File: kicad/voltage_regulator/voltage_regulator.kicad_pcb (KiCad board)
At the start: 2 copper layers, 135.9 x 78.7 mm, 18 parts

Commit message: New commit.
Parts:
- moved XS2 26.2 mm to (178.4, 96.3)
- moved C6 20.9 mm to (171.4, 122.9)
- moved C3 20.9 mm to (171.4, 89.9)
- moved C2 19.1 mm to (153.0, 80.4)
- moved 1_PIN 18.6 mm to (182.9, 65.8)
- moved FU1 17.8 mm to (101.0, 85.5)
- moved 1_PIN 17.6 mm to (182.9, 122.9)
- moved C1 17.5 mm to (121.9, 80.4)
- moved C5 17.2 mm to (153.0, 112.1)
- moved C4 15.5 mm to (121.9, 112.1)
- moved VD1 13.8 mm to (93.3, 71.5), turned to 180 degrees
- moved FU2 12.8 mm to (101.0, 107.1)
- moved VD2 12.3 mm to (90.2, 80.4), turned to 270 degrees
- moved 1_PIN 11.0 mm to (76.2, 124.8)
- moved XS1 10.0 mm to (91.4, 96.3)
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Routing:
- net /GND: track 180.3 -> 23.5 mm
- net /VCC+: track 146.6 -> 4.45 mm
- net /VCC-: track 142.4 -> 4.32 mm
- net N-000004: track 80.1 -> 59.2 mm
- net N-000006: track 28.8 -> 9.79 mm
- net N-000005: track 28.8 -> 9.90 mm
- net N-000003: track 69.2 -> 59.5 mm
- added copper zone on B.Cu, net /GND
- added copper zone on F.Cu, net /VCC+
- added copper zone on B.Cu, net /VCC-
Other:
- board size 135.9 x 78.7 mm -> 101 x 63.5 mm
- net class Default: clearance 1.00076 -> 0.5; trace_width 0.50038 -> 1
- rule trace_clearance: 1.00076 -> 0.5
- board text added: "GND"
- board text added: "VCC"
- board text added: "VCC+"
- board text added: "VCC-"

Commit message: New commit.
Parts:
- moved VD4 8.00 mm to (93.3, 113.0)
- moved VD1 7.87 mm to (93.3, 79.4)
- moved VD2 2.16 mm to (88.3, 79.4), turned to 180 degrees
- moved VD3 2.10 mm to (88.3, 113.0), turned to 180 degrees
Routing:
- net /GND: track 23.5 -> 47.0 mm
- net N-000004: track 59.2 -> 68.7 mm
- net N-000003: track 59.5 -> 67.9 mm
- added copper zone on F.Cu, net /GND
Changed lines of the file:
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@@
     (thickness 1.6002)
     (drawings 10)
-    (tracks 25)
+    (tracks 29)
     (zones 0)
     (modules 18)
@@
   )
   (module TO220_DIOD_VERT_POZ (layer Front)
-    (at 93.345 121.031 180)
+    (at 93.345 113.03 180)
     (descr "Regulateur TO220 serie LM78xx")
     (tags "TR TO220")
-    (fp_text reference VD4 (at 3.81 3.81 270) (layer F.SilkS)
+    (fp_text reference VD4 (at 0.127 6.223 180) (layer F.SilkS)
       (effects (font (size 1.524 1.016) (thickness 0.2032)))
     )
@@
   )
   (module TO220_DIOD_VERT_POZ (layer Front)
-    (at 93.345 71.501 180)
+    (at 93.345 79.375 180)
     (descr "Regulateur TO220 serie LM78xx")
     (tags "TR TO220")
-    (fp_text reference VD1 (at 3.81 -3.81 270) (layer F.SilkS)
+    (fp_text reference VD1 (at 0 -6.604 180) (layer F.SilkS)
       (effects (font (size 1.524 1.016) (thickness 0.2032)))
     )
@@
   )
   (module TO220_DIOD_VERT_POZ (layer Front)
-    (at 90.17 80.391 270)
+    (at 88.265 79.375 180)
     (descr "Regulateur TO220 serie LM78xx")
     (tags "TR TO220")
-    (fp_text reference VD2 (at 0 6.35 270) (layer F.SilkS)
-      (effects (font (size 1.524 1.016) (thickness 0.2032)))
-    )
-    (fp_text value MDR10100 (at -3.81 0 360) (layer F.SilkS) hide
+    (fp_text reference VD2 (at 0 -6.604 180) (layer F.SilkS)
+      (effects (font (size 1.524 1.016) (thickness 0.2032)))
+    )
+    (fp_text value MDR10100 (at -3.81 0 270) (layer F.SilkS) hide
       (effects (font (size 1.524 1.016) (thickness 0.2032)))
     )
@@
     (fp_line (start 1.905 5.08) (end -1.905 5.08) (layer F.SilkS) (width 0.381))
     (fp_line (start -1.905 5.08) (end -1.905 -5.08) (layer F.SilkS) (width 0.381))
-    (pad 2 thru_hole rect (at 0 -2.54 270) (size 1.778 1.778) (drill 1.00076)
+    (pad 2 thru_hole rect (at 0 -2.54 180) (size 1.778 1.778) (drill 1.00076)
       (layers *.Cu *.Mask F.SilkS)
       (net 2 /VCC+)
     )
-    (pad 1 thru_hole circle (at 0 2.54 270) (size 1.778 1.778) (drill 1.00076)
+    (pad 1 thru_hole circle (at 0 2.54 180) (size 1.778 1.778) (drill 1.00076)
       (layers *.Cu *.Mask F.SilkS)
       (net 5 N-000004)
@@
   )
   (module TO220_DIOD_VERT_POZ (layer Front)
-    (at 90.17 112.141 90)
+    (at 88.265 113.03 180)
     (descr "Regulateur TO220 serie LM78xx")
     (tags "TR TO220")
-    (fp_text reference VD3 (at 0 -6.35 90) (layer F.SilkS)
-      (effects (font (size 1.524 1.016) (thickness 0.2032)))
-    )
-    (fp_text value MDR10100 (at -3.81 0 180) (layer F.SilkS) hide
+    (fp_text reference VD3 (at 0.127 6.35 180) (layer F.SilkS)
+      (effects (font (size 1.524 1.016) (thickness 0.2032)))
+    )
+    (fp_text value MDR10100 (at -3.81 0 270) (layer F.SilkS) hide
       (effects (font (size 1.524 1.016) (thickness 0.2032)))
     )
@@
     (fp_line (start 1.905 5.08) (end -1.905 5.08) (layer F.SilkS) (width 0.381))
     (fp_line (start -1.905 5.08) (end -1.905 -5.08) (layer F.SilkS) (width 0.381))
-    (pad 2 thru_hole rect (at 0 -2.54 90) (size 1.778 1.778) (drill 1.00076)
+    (pad 2 thru_hole rect (at 0 -2.54 180) (size 1.778 1.778) (drill 1.00076)
       (layers *.Cu *.Mask F.SilkS)
       (net 4 N-000003)
     )
-    (pad 1 thru_hole circle (at 0 2.54 90) (size 1.778 1.778) (drill 1.00076)
+    (pad 1 thru_hole circle (at 0 2.54 180) (size 1.778 1.778) (drill 1.00076)
       (layers *.Cu *.Mask F.SilkS)
       (net 3 /VCC-)
@@
   (gr_line (start 182.915 64.516) (end 81.915 64.516) (angle 90) (layer Edge.Cuts) (width 0.381))
   (gr_line (start 81.915 128.016) (end 182.915 128.016) (angle 90) (layer Edge.Cuts) (width 0.381))
-  (gr_text VCC (at 91.44 106.426) (layer F.SilkS)
+  (gr_text VCC (at 85.09 101.6) (layer F.SilkS)
     (effects (font (size 2.032 1.524) (thickness 0.3048)))
   )
   (gr_line (start 182.915 128.016) (end 182.915 64.516) (angle 90) (layer Edge.Cuts) (width 0.381))
   (gr_line (start 81.915 128.016) (end 81.915 64.516) (angle 90) (layer Edge.Cuts) (width 0.381))
-  (gr_text GND (at 85.725 96.266 90) (layer F.SilkS)
+  (gr_text GND (at 85.09 96.52) (layer F.SilkS)
     (effects (font (size 2.032 1.524) (thickness 0.3048)))
   )
-  (gr_text VCC (at 91.44 86.741) (layer F.SilkS)
+  (gr_text VCC (at 85.09 91.44) (layer F.SilkS)
     (effects (font (size 2.032 1.524) (thickness 0.3048)))
   )
@@
     (effects (font (size 2.032 1.524) (thickness 0.3048)))
   )
+  (segment (start 91.44 96.266) (end 109.855 96.266) (width 5) (layer Front) (net 1))
+  (segment (start 178.435 96.266) (end 173.355 96.266) (width 5) (layer Front) (net 1))
   (segment (start 178.435 96.266) (end 173.355 96.266) (width 5) (layer Back) (net 1))
   (segment (start 91.44 96.266) (end 109.855 96.266) (width 5) (layer Back) (net 1))
   (segment (start 178.435 91.186) (end 178.435 86.741) (width 4) (layer Front) (net 2))
   (segment (start 178.435 101.346) (end 178.435 105.664) (width 4) (layer Back) (net 3))
-  (segment (start 100.965 68.961) (end 100.965 78.359) (width 4) (layer Back) (net 4))
-  (segment (start 87.63 104.648) (end 87.63 112.141) (width 4) (layer Back) (net 4))
-  (segment (start 86.36 103.378) (end 87.63 104.648) (width 4) (layer Back) (net 4))
-  (segment (start 86.36 89.408) (end 86.36 103.378) (width 4) (layer Back) (net 4))
-  (segment (start 90.043 85.725) (end 86.36 89.408) (width 4) (layer Back) (net 4))
-  (segment (start 93.599 85.725) (end 90.043 85.725) (width 4) (layer Back) (net 4))
-  (segment (start 100.965 78.359) (end 93.599 85.725) (width 4) (layer Back) (net 4))
-  (segment (start 100.965 68.961) (end 93.345 68.961) (width 4) (layer Back) (net 4))
-  (segment (start 87.63 80.391) (end 87.63 88.138) (width 4) (layer Front) (net 5))
-  (segment (start 100.965 114.808) (end 100.965 123.571) (width 4) (layer Front) (net 5))
-  (segment (start 93.726 107.569) (end 100.965 114.808) (width 4) (layer Front) (net 5))
-  (segment (start 90.551 107.569) (end 93.726 107.569) (width 4) (layer Front) (net 5))
-  (segment (start 86.36 103.378) (end 90.551 107.569) (width 4) (layer Front) (net 5))
-  (segment (start 86.36 89.408) (end 86.36 103.378) (width 4) (layer Front) (net 5))
-  (segment (start 87.63 88.138) (end 86.36 89.408) (width 4) (layer Front) (net 5))
-  (segment (start 93.345 123.571) (end 100.965 123.571) (width 4) (layer Back) (net 5))
+  (segment (start 93.345 76.835) (end 100.965 76.835) (width 4) (layer Back) (net 4) (status 400000))
+  (segment (start 88.265 115.57) (end 86.106 115.57) (width 4) (layer Back) (net 4) (status 400000))
+  (segment (start 100.965 80.137) (end 100.965 76.835) (width 4) (layer Back) (net 4))
+  (segment (start 100.965 76.835) (end 100.965 68.961) (width 4) (layer Back) (net 4) (status 800000))
+  (segment (start 95.25 85.852) (end 100.965 80.137) (width 4) (layer Back) (net 4))
+  (segment (start 88.519 85.852) (end 95.25 85.852) (width 4) (layer Back) (net 4))
+  (segment (start 84.455 89.916) (end 88.519 85.852) (width 4) (layer Back) (net 4))
+  (segment (start 84.455 113.919) (end 84.455 89.916) (width 4) (layer Back) (net 4))
+  (segment (start 86.106 115.57) (end 84.455 113.919) (width 4) (layer Back) (net 4))
+  (segment (start 93.345 115.57) (end 100.965 115.57) (width 4) (layer Front) (net 5) (status 400000))
+  (segment (start 88.265 76.835) (end 86.233 76.835) (width 4) (layer Front) (net 5) (status 400000))
+  (segment (start 100.965 112.522) (end 100.965 115.57) (width 4) (layer Front) (net 5))
+  (segment (start 100.965 115.57) (end 100.965 123.571) (width 4) (layer Front) (net 5) (status 800000))
+  (segment (start 94.869 106.426) (end 100.965 112.522) (width 4) (layer Front) (net 5))
+  (segment (start 86.868 106.426) (end 94.869 106.426) (width 4) (layer Front) (net 5))
+  (segment (start 84.455 104.013) (end 86.868 106.426) (width 4) (layer Front) (net 5))
+  (segment (start 84.455 78.613) (end 84.455 104.013) (width 4) (layer Front) (net 5))
+  (segment (start 86.233 76.835) (end 84.455 78.613) (width 4) (layer Front) (net 5))
   (segment (start 100.965 101.981) (end 92.154998 101.981) (width 4) (layer Back) (net 6))
   (segment (start 91.44 101.266002) (end 91.44 101.346) (width 4) (layer Back) (net 6))
@@
       (pts
         (xy 180.34 89.281) (xy 176.53 89.281) (xy 173.99 82.931) (xy 155.575 77.851) (xy 119.38 77.851)
-        (xy 114.173 81.661) (xy 91.821 81.661) (xy 91.821 81.026) (xy 91.821 72.771) (xy 108.585 72.771)
-        (xy 114.935 67.056) (xy 171.45 67.056) (xy 173.99 69.596) (xy 180.467 76.708)
+        (xy 110.998 83.82) (xy 94.615 83.82) (xy 94.615 83.82) (xy 86.868 83.82) (xy 86.868 80.01)
+        (xy 94.615 80.01) (xy 94.742 80.01) (xy 114.935 67.056) (xy 171.45 67.056) (xy 173.99 69.596)
+        (xy 180.467 76.708)
+      )
+    )
+  )
+  (zone (net 1) (net_name /GND) (layer Front) (hatch edge 0.508)
+    (connect_pads yes (clearance 1))
+    (min_thickness 0.5)
+    (fill (arc_segments 16) (thermal_gap 0.508) (thermal_bridge_width 0.508))
+    (polygon
+      (pts
+        (xy 105.41 93.726) (xy 119.38 82.931) (xy 155.575 82.931) (xy 173.355 88.011) (xy 174.625 93.726)
+        (xy 174.625 98.806) (xy 173.355 104.521) (xy 155.575 109.601) (xy 119.38 109.601) (xy 105.41 98.806)
       )
     )
@@
     (polygon
       (pts
-        (xy 180.467 103.251) (xy 176.657 103.251) (xy 173.99 109.601) (xy 155.575 114.681) (xy 119.38 114.681)
-        (xy 114.173 110.871) (xy 92.075 110.871) (xy 91.313 110.871) (xy 91.313 119.761) (xy 108.585 119.761)
-        (xy 114.935 125.476) (xy 171.45 125.476) (xy 173.99 122.936) (xy 180.467 116.078)
+        (xy 180.34 103.251) (xy 176.53 103.251) (xy 173.99 109.601) (xy 155.575 114.681) (xy 119.38 114.681)
+        (xy 110.998 108.712) (xy 94.615 108.712) (xy 94.615 108.712) (xy 86.868 108.712) (xy 86.868 112.522)
+        (xy 94.615 112.522) (xy 94.742 112.522) (xy 114.935 125.476) (xy 171.45 125.476) (xy 173.99 122.936)
+        (xy 180.467 115.824)
       )
     )

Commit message: New commit.
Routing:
- net /GND: track 47.0 -> 23.5 mm
- removed copper zone on F.Cu, net /GND
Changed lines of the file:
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@@
     (thickness 1.6002)
     (drawings 10)
-    (tracks 29)
+    (tracks 27)
     (zones 0)
     (modules 18)
@@
   )
   (setup
-    (last_trace_width 4)
+    (last_trace_width 1)
     (user_trace_width 2)
     (user_trace_width 4)
@@
     (effects (font (size 2.032 1.524) (thickness 0.3048)))
   )
-  (segment (start 91.44 96.266) (end 109.855 96.266) (width 5) (layer Front) (net 1))
-  (segment (start 178.435 96.266) (end 173.355 96.266) (width 5) (layer Front) (net 1))
   (segment (start 178.435 96.266) (end 173.355 96.266) (width 5) (layer Back) (net 1))
   (segment (start 91.44 96.266) (end 109.855 96.266) (width 5) (layer Back) (net 1))
   (segment (start 178.435 91.186) (end 178.435 86.741) (width 4) (layer Front) (net 2))
   (segment (start 178.435 101.346) (end 178.435 105.664) (width 4) (layer Back) (net 3))
-  (segment (start 93.345 76.835) (end 100.965 76.835) (width 4) (layer Back) (net 4) (status 400000))
-  (segment (start 88.265 115.57) (end 86.106 115.57) (width 4) (layer Back) (net 4) (status 400000))
+  (segment (start 93.345 76.835) (end 100.965 76.835) (width 4) (layer Back) (net 4))
+  (segment (start 88.265 115.57) (end 86.106 115.57) (width 4) (layer Back) (net 4))
   (segment (start 100.965 80.137) (end 100.965 76.835) (width 4) (layer Back) (net 4))
-  (segment (start 100.965 76.835) (end 100.965 68.961) (width 4) (layer Back) (net 4) (status 800000))
+  (segment (start 100.965 76.835) (end 100.965 68.961) (width 4) (layer Back) (net 4))
   (segment (start 95.25 85.852) (end 100.965 80.137) (width 4) (layer Back) (net 4))
   (segment (start 88.519 85.852) (end 95.25 85.852) (width 4) (layer Back) (net 4))
@@
   (segment (start 84.455 113.919) (end 84.455 89.916) (width 4) (layer Back) (net 4))
   (segment (start 86.106 115.57) (end 84.455 113.919) (width 4) (layer Back) (net 4))
-  (segment (start 93.345 115.57) (end 100.965 115.57) (width 4) (layer Front) (net 5) (status 400000))
-  (segment (start 88.265 76.835) (end 86.233 76.835) (width 4) (layer Front) (net 5) (status 400000))
+  (segment (start 93.345 115.57) (end 100.965 115.57) (width 4) (layer Front) (net 5))
+  (segment (start 88.265 76.835) (end 86.233 76.835) (width 4) (layer Front) (net 5))
   (segment (start 100.965 112.522) (end 100.965 115.57) (width 4) (layer Front) (net 5))
-  (segment (start 100.965 115.57) (end 100.965 123.571) (width 4) (layer Front) (net 5) (status 800000))
+  (segment (start 100.965 115.57) (end 100.965 123.571) (width 4) (layer Front) (net 5))
   (segment (start 94.869 106.426) (end 100.965 112.522) (width 4) (layer Front) (net 5))
   (segment (start 86.868 106.426) (end 94.869 106.426) (width 4) (layer Front) (net 5))
@@
       )
     )
-  )
-  (zone (net 1) (net_name /GND) (layer Front) (hatch edge 0.508)
-    (connect_pads yes (clearance 1))
-    (min_thickness 0.5)
-    (fill (arc_segments 16) (thermal_gap 0.508) (thermal_bridge_width 0.508))
-    (polygon
-      (pts
-        (xy 105.41 93.726) (xy 119.38 82.931) (xy 155.575 82.931) (xy 173.355 88.011) (xy 174.625 93.726)
-        (xy 174.625 98.806) (xy 173.355 104.521) (xy 155.575 109.601) (xy 119.38 109.601) (xy 105.41 98.806)
-      )
-    )

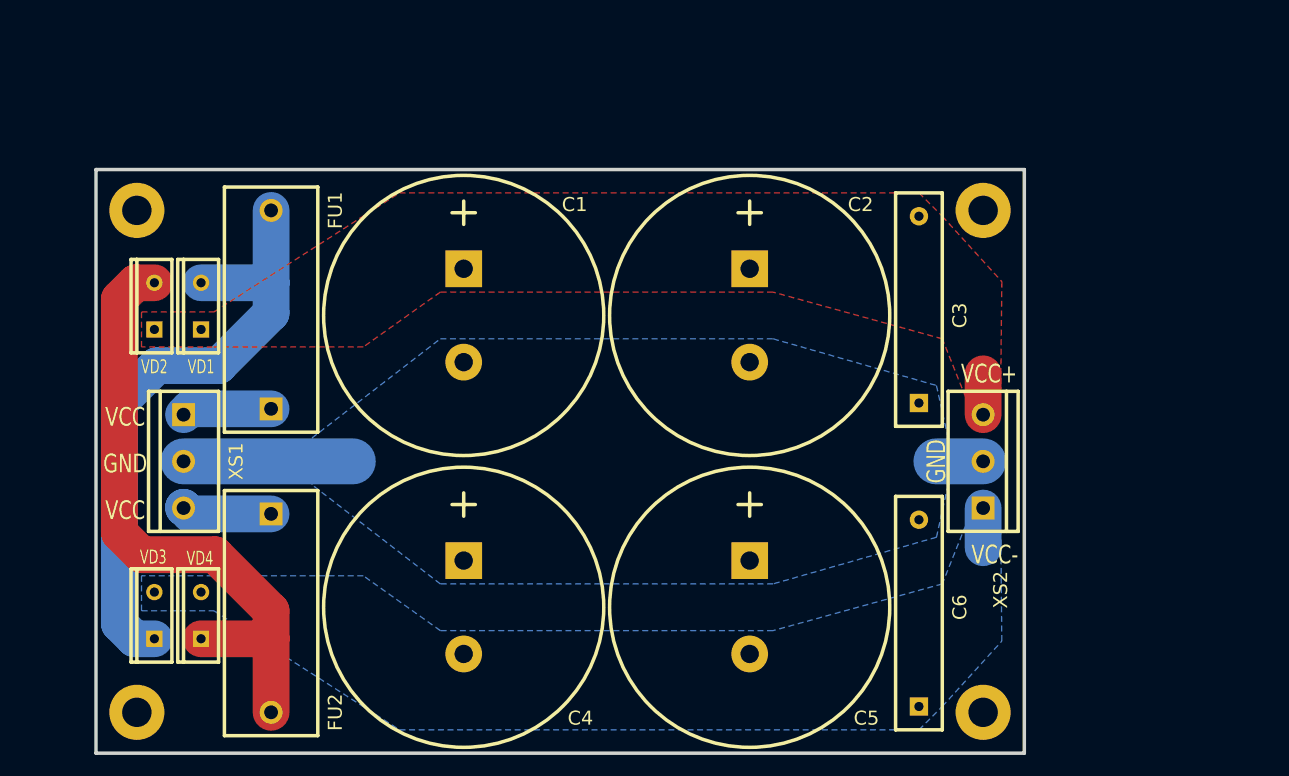
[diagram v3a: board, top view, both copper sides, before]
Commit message: Add emc filter.
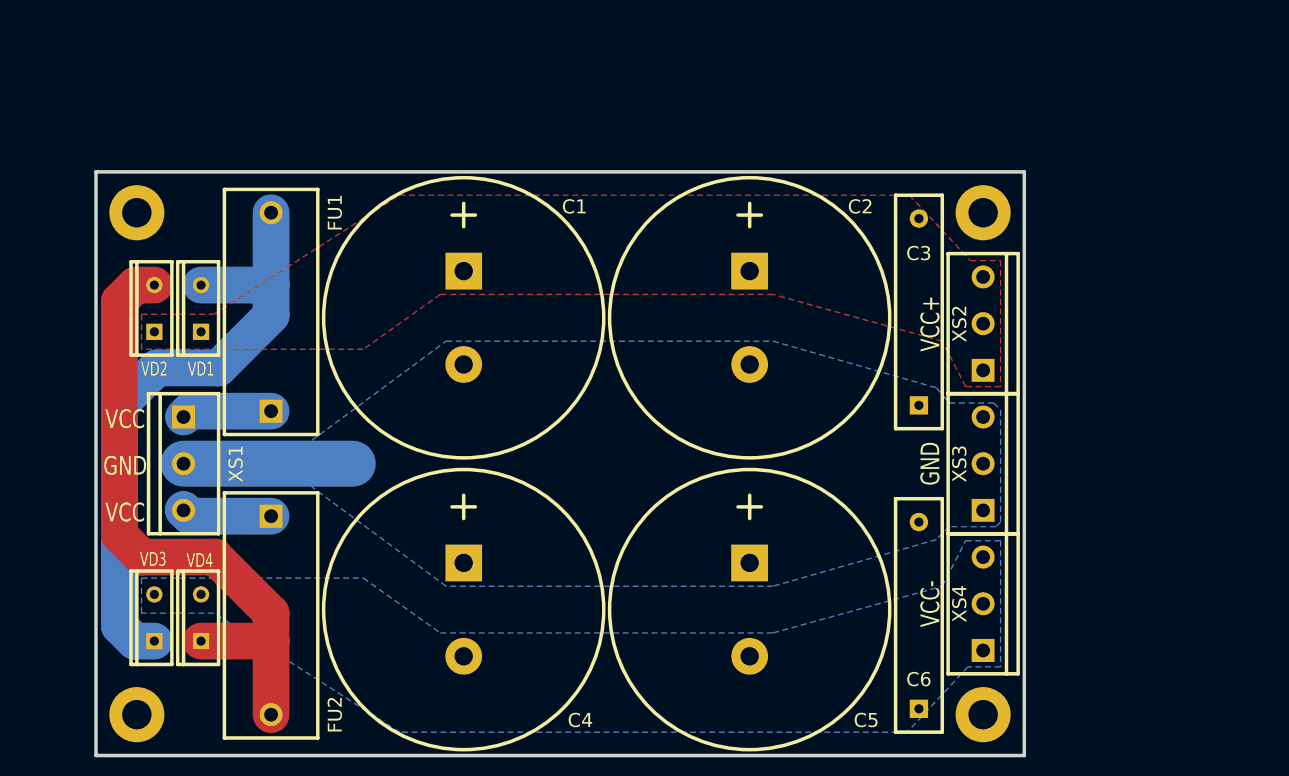
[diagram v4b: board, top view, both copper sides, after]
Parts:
- added XS3: DG126-5.0-03P-14, DG126-5.0-03P-14, F.Cu at (178.4, 96.5)
- added XS4: DG126-5.0-03P-14, DG126-5.0-03P-14, F.Cu at (178.4, 111.8)
- C1, C2, C4, C5: value 10000_мк_50_В -> 10000 мк 63 В
- C3, C6: value 0.22_мк_400_В -> 0.47мк 400В
- FU1, FU2: value 10_A -> 10 A
- VD1, VD2, VD3, VD4: value MDR10100 -> MBR10100
- moved XS2 15.0 mm to (178.4, 81.3)
- moved 1_PIN 0.25 mm to (182.9, 66.0)
- moved 1_PIN 0.25 mm to (76.2, 125.1)
- moved C3 0.25 mm to (171.4, 90.2)
- moved VD1 0.25 mm to (93.3, 79.6)
- moved VD2 0.25 mm to (88.3, 79.6)
- moved VD3 0.25 mm to (88.3, 113.3)
- moved VD4 0.25 mm to (93.3, 113.3)
- moved 1_PIN 0.25 mm to (182.9, 123.2)
- moved 1_PIN 0.25 mm to (81.9, 66.7)
- moved C1 0.25 mm to (121.9, 80.6)
- moved C2 0.25 mm to (153.0, 80.6)
- moved C4 0.25 mm to (121.9, 112.4)
- moved C5 0.25 mm to (153.0, 112.4)
- moved C6 0.25 mm to (171.4, 123.2)
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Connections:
- XS2 pad 1: /VCC- -> /VCC+
- XS2 pad 2: /GND -> /VCC+
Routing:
- net /GND: track 23.5 -> 18.4 mm
- net /VCC+: track 4.45 -> 0.00 mm
- net /VCC-: track 4.32 -> 0.00 mm

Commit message: Add 2 way active filter.
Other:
- board text added: "AC"
- board text added: "DC+"
- board text added: "DC-"
- board text removed: "VCC"
- board text removed: "VCC+"
- board text removed: "VCC-"
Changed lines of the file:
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@@
   (gr_line (start 182.915 64.77) (end 81.915 64.77) (angle 90) (layer Edge.Cuts) (width 0.381))
   (gr_line (start 81.915 128.27) (end 182.915 128.27) (angle 90) (layer Edge.Cuts) (width 0.381))
-  (gr_text VCC (at 85.09 101.854) (layer F.SilkS)
+  (gr_text AC (at 85.09 101.854) (layer F.SilkS)
     (effects (font (size 2.032 1.524) (thickness 0.3048)))
   )
@@
     (effects (font (size 2.032 1.524) (thickness 0.3048)))
   )
-  (gr_text VCC (at 85.09 91.694) (layer F.SilkS)
+  (gr_text AC (at 85.09 91.694) (layer F.SilkS)
     (effects (font (size 2.032 1.524) (thickness 0.3048)))
   )
@@
     (effects (font (size 2.032 1.524) (thickness 0.3048)))
   )
-  (gr_text VCC- (at 172.72 111.76 90) (layer F.SilkS)
+  (gr_text DC- (at 172.72 111.76 90) (layer F.SilkS)
     (effects (font (size 2.032 1.524) (thickness 0.3048)))
   )
-  (gr_text VCC+ (at 172.72 81.28 90) (layer F.SilkS)
+  (gr_text DC+ (at 172.72 81.28 90) (layer F.SilkS)
     (effects (font (size 2.032 1.524) (thickness 0.3048)))
   )
